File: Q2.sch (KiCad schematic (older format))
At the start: 55 parts, among them U1 LM317, U10 SP-2U1+, U11 SMA, U12 LT1009, U13 TL974, U2 Teensy3.2, U3 SMA, U4 ROS-2536C-119+, U5 PMA4-33GLN+, U6 PGA-103+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

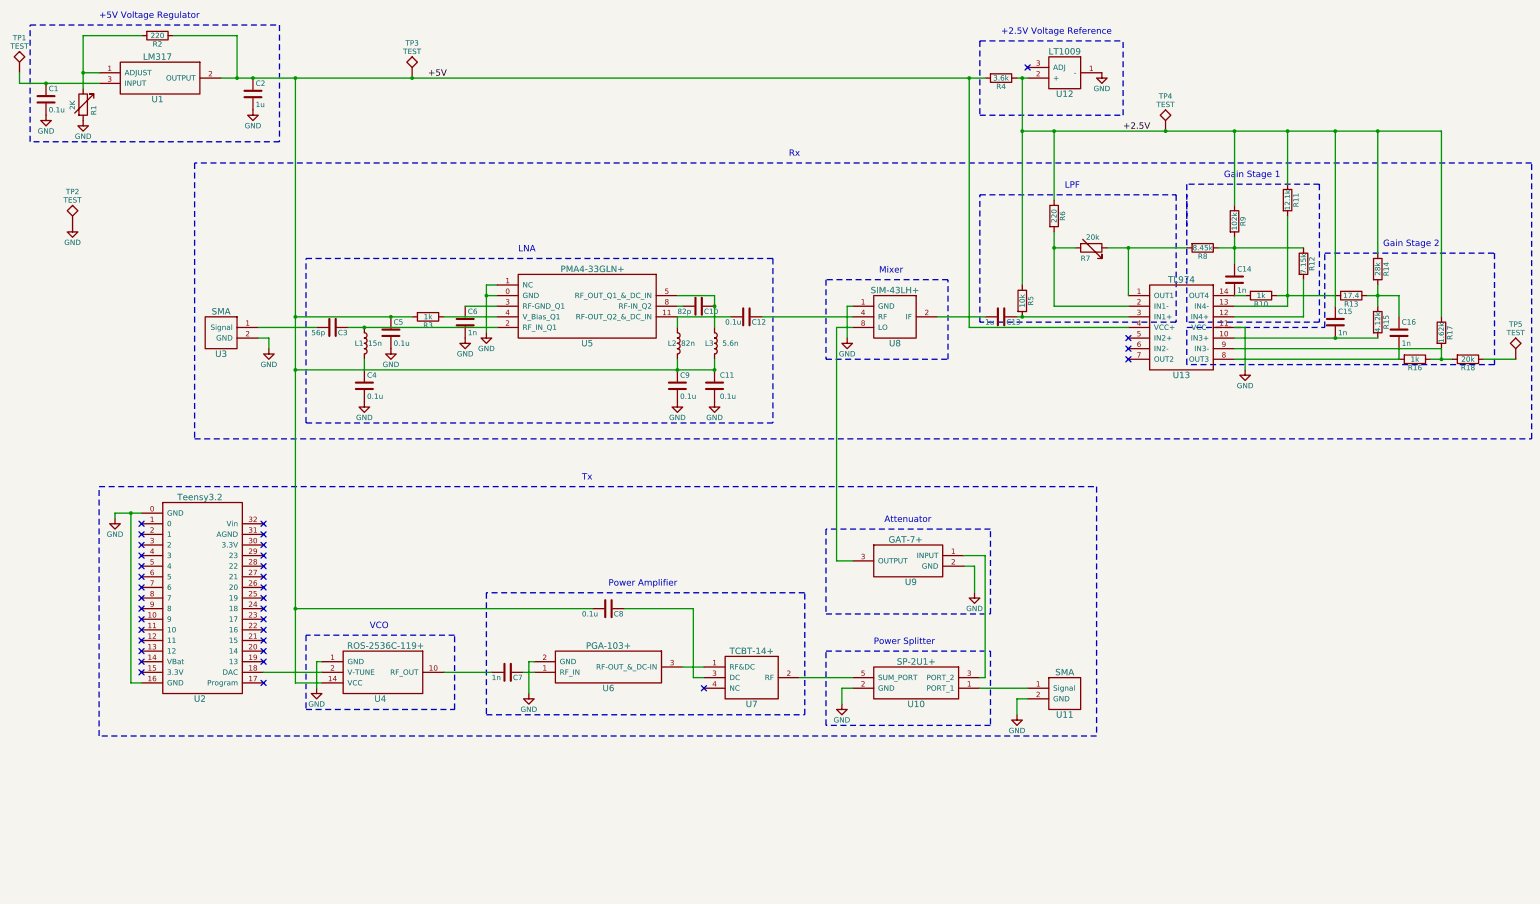
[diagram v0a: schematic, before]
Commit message: Update
Fixed Missing LNA
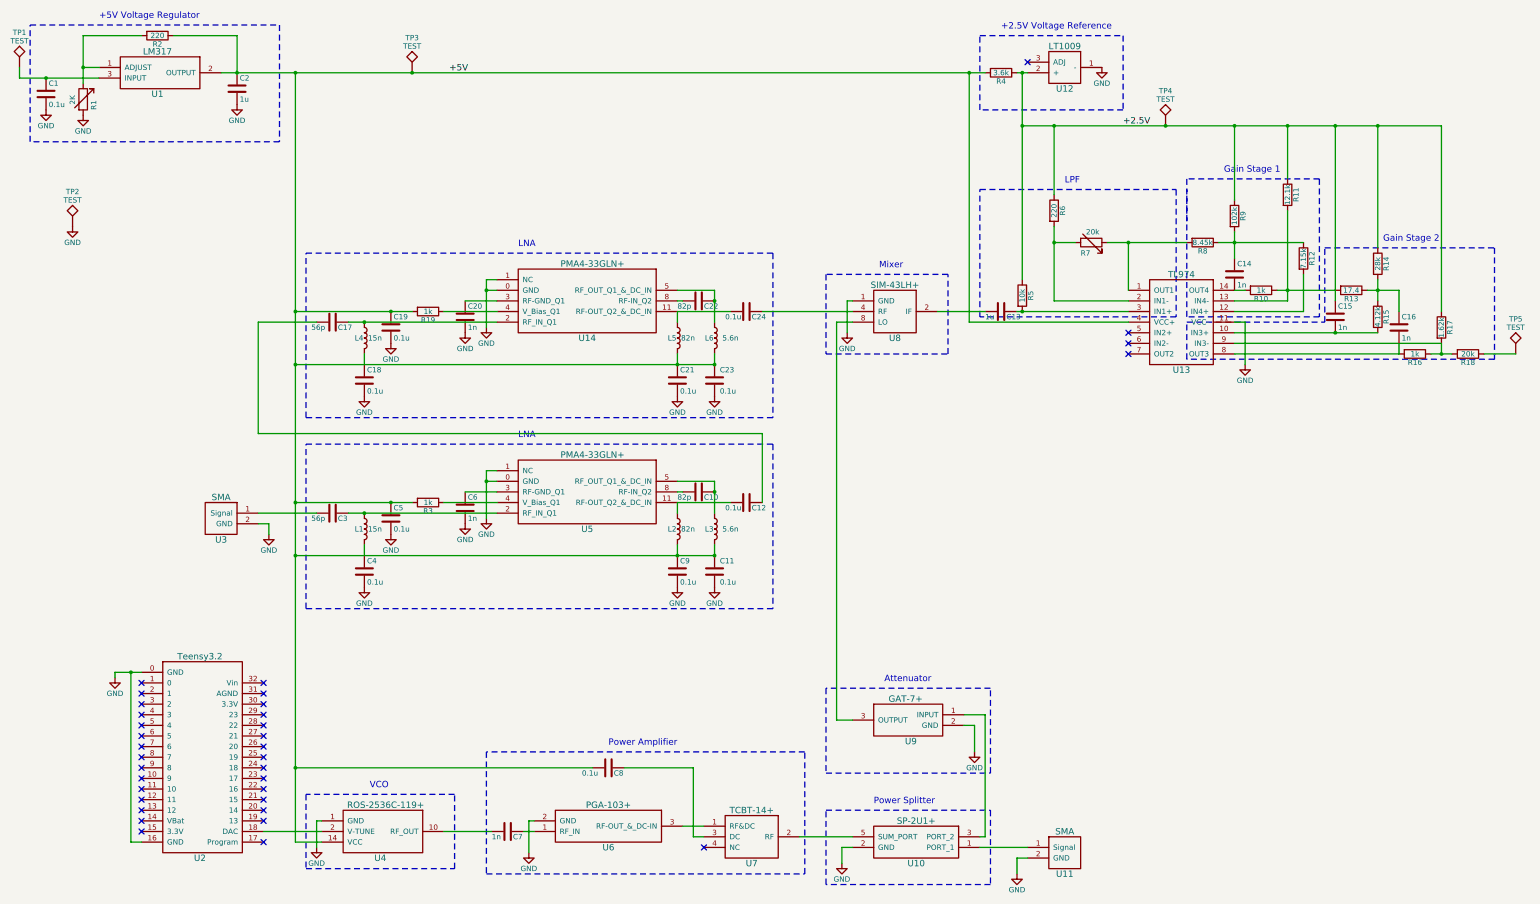
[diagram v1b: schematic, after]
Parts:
- added C17: 56p, Q2Footprint:C_0805_HandSoldering, symbol C
- added C18, C19, C21, C23, C24: 0.1u, Q2Footprint:C_0805_HandSoldering, symbol C
- added C20: 1n, Q2Footprint:C_0805_HandSoldering, symbol C
- added C22: 82p, Q2Footprint:C_0805_HandSoldering, symbol C
- added L4: 15n, Q2Footprint:L_0805_HandSoldering, symbol L
- added L5: 82n, Q2Footprint:L_0805_HandSoldering, symbol L
- added L6: 5.6n, Q2Footprint:L_0805_HandSoldering, symbol L
- added R19: 1k, Q2Footprint:R_0805_HandSoldering, symbol R
- added U14: PMA4-33GLN+, Q2Footprint:PMA4-33GLN+, symbol PMA4-33GLN+
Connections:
- net +5V: now also C19.1, C21.1, C23.1, L5.2, L6.2, R19.2
- net GND: now also C18.2, C19.2, C20.2, C21.2, C23.2, U14.0 (GND), U14.1 (NC)
- net at C12.1: now also C17.2; no longer U8.4 (RF)
- new net: C24.2, L5.1, U14.11 (RF-OUT_Q2_&_DC_IN)
- new net: C17.1, L4.1, U14.2 (RF_IN_Q1)
- new net: C20.1, U14.3 (RF-GND_Q1)
- new net: R19.1, U14.4 (V_Bias_Q1)
- new net: C22.1, L6.1, U14.5 (RF_OUT_Q1_&_DC_IN)
- new net: C22.2, U14.8 (RF-IN_Q2)
- new net: C18.1, L4.2
- new net: C24.1, U8.4 (RF)
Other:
- note removed: "Rx"
- note removed: "Tx"
- moved on the sheet: C1, C10, C11, C12, C13, C14, C15, C16, C2, C3, C4, C5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

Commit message: Update
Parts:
- C12, C24: value 0.1u -> 68p
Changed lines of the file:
@@
 P 7400 5450
 F 0 "C12" V 7450 5500 50  0000 L CNN
-F 1 "0.1u" V 7450 5250 50  0000 L CNN
+F 1 "68p" V 7450 5250 50  0000 L CNN
 F 2 "Q2Footprint:C_0805_HandSoldering" H 7438 5300 50  0001 C CNN
 F 3 "" H 7400 5450 50  0001 C CNN
@@
 P 7400 3650
 F 0 "C24" V 7450 3700 50  0000 L CNN
-F 1 "0.1u" V 7450 3450 50  0000 L CNN
+F 1 "68p" V 7450 3450 50  0000 L CNN
 F 2 "Q2Footprint:C_0805_HandSoldering" H 7438 3500 50  0001 C CNN
 F 3 "" H 7400 3650 50  0001 C CNN

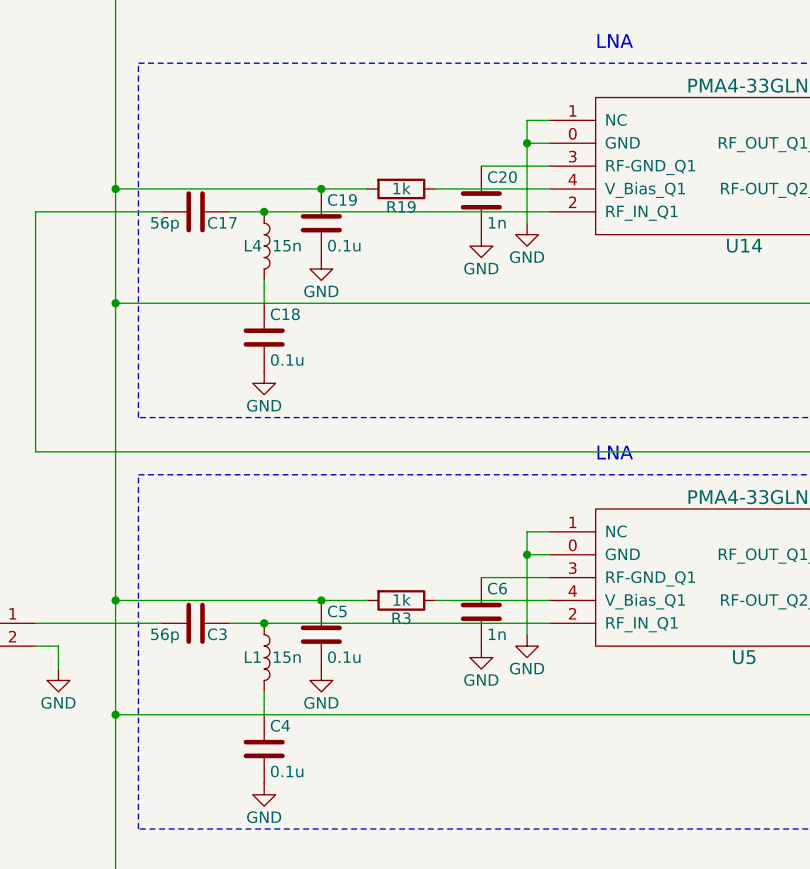
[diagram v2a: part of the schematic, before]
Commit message: Update
Fixed LNA Connection
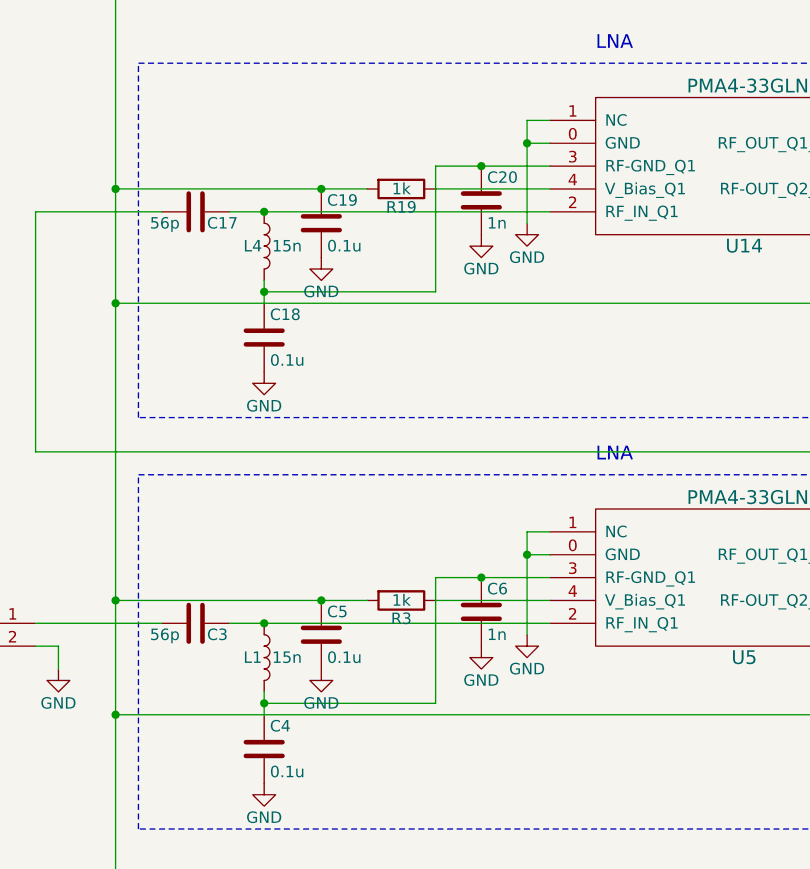
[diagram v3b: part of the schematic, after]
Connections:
- net at C6.1, U5.3 (RF-GND_Q1): now also C4.1, L1.2
- net at C20.1, U14.3 (RF-GND_Q1): now also C18.1, L4.2

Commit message: Update
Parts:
- added C25: 1n, Q2Footprint:C_0805_HandSoldering, symbol C
- R13: value 17.4 -> 17.4k
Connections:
- net +2.5V: now also C25.1
- net at R12.2, U13.12 (IN4+): now also C25.2
- net at C16.2, U13.8 (OUT3): now also R16.1, R18.2; no longer R16.2
- net at R17.2, U13.9 (IN3-): now also R16.2; no longer R16.1, R18.2
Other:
- moved on the sheet: C16, R16, R17
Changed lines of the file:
@@
 P 13100 3450
 F 0 "R13" V 13180 3450 50  0000 C CNN
-F 1 "17.4" V 13100 3450 50  0000 C CNN
+F 1 "17.4k" V 13100 3450 50  0000 C CNN
 F 2 "Q2Footprint:R_0805_HandSoldering" V 13030 3450 50  0001 C CNN
 F 3 "" H 13100 3450 50  0001 C CNN
@@
 L C C16
 U 1 1 5A7C3B98
-P 13550 3800
-F 0 "C16" H 13575 3900 50  0000 L CNN
-F 1 "1n" H 13575 3700 50  0000 L CNN
-F 2 "Q2Footprint:C_0805_HandSoldering" H 13588 3650 50  0001 C CNN
-F 3 "" H 13550 3800 50  0001 C CNN
-	1    13550 3800
+P 13550 3750
+F 0 "C16" H 13575 3850 50  0000 L CNN
+F 1 "1n" H 13575 3650 50  0000 L CNN
+F 2 "Q2Footprint:C_0805_HandSoldering" H 13588 3600 50  0001 C CNN
+F 3 "" H 13550 3750 50  0001 C CNN
+	1    13550 3750
 	1    0    0    -1
 $EndComp
@@
 L R R17
 U 1 1 5A7C5FF9
-P 13950 3800
-F 0 "R17" V 14030 3800 50  0000 C CNN
-F 1 "1.62k" V 13950 3800 50  0000 C CNN
-F 2 "Q2Footprint:R_0805_HandSoldering" V 13880 3800 50  0001 C CNN
-F 3 "" H 13950 3800 50  0001 C CNN
-	1    13950 3800
+P 13900 3450
+F 0 "R17" V 13980 3450 50  0000 C CNN
+F 1 "1.62k" V 13900 3450 50  0000 C CNN
+F 2 "Q2Footprint:R_0805_HandSoldering" V 13830 3450 50  0001 C CNN
+F 3 "" H 13900 3450 50  0001 C CNN
+	1    13900 3450
 	1    0    0    -1
 $EndComp
@@
 L R R16
 U 1 1 5A7C6A64
-P 13700 4050
-F 0 "R16" V 13780 4050 50  0000 C CNN
-F 1 "1k" V 13700 4050 50  0000 C CNN
-F 2 "Q2Footprint:R_0805_HandSoldering" V 13630 4050 50  0001 C CNN
-F 3 "" H 13700 4050 50  0001 C CNN
-	1    13700 4050
-	0    1    1    0
+P 14050 3850
+F 0 "R16" V 14130 3850 50  0000 C CNN
+F 1 "1k" V 14050 3850 50  0000 C CNN
+F 2 "Q2Footprint:R_0805_HandSoldering" V 13980 3850 50  0001 C CNN
+F 3 "" H 14050 3850 50  0001 C CNN
+	1    14050 3850
+	-1   0    0    1
 $EndComp
 $Comp
@@
 	8250 3750 8400 3750
 Wire Wire Line
-	8250 3750 8250 7500
-Wire Wire Line
 	8250 7500 8400 7500
 Wire Wire Line
@@
 	6750 5250 7100 5250
 Wire Wire Line
-	3800 5950 3800 5850
+	3800 5850 3800 5950
 Wire Wire Line
 	14650 4050 14350 4050
 Connection ~ 3800 5550
 Wire Wire Line
-	3800 5550 3800 5550
-Wire Wire Line
 	3650 5550 5050 5550
 Wire Wire Line
@@
 Wire Notes Line
 	12850 3050 14450 3050
-Connection ~ 13950 4050
-Wire Wire Line
-	13950 3950 13950 4050
-Wire Wire Line
-	13850 4050 14050 4050
-Wire Wire Line
-	13950 3950 12000 3950
 Connection ~ 13350 1900
 Wire Wire Line
-	13950 1900 13950 3650
-Wire Wire Line
-	13550 4050 12000 4050
-Wire Wire Line
-	13550 3950 13550 4050
-Wire Wire Line
-	13550 3450 13550 3650
+	13900 1900 13900 3300
+Wire Wire Line
+	12000 4050 14050 4050
 Connection ~ 12950 3850
 Connection ~ 12950 1900
@@
 Wire Wire Line
 	13350 3350 13350 3550
-Wire Wire Line
-	13250 3450 13550 3450
 Wire Notes Line
 	12800 3700 11550 3700
@@
 	10300 1900 10300 2550
 Wire Wire Line
-	10000 1900 13950 1900
+	10000 1900 13900 1900
 Wire Wire Line
 	10800 3000 11550 3000
@@
 	6750 3450 7100 3450
 Wire Wire Line
-	3800 4150 3800 4050
+	3800 4050 3800 4150
 Connection ~ 3800 3750
-Wire Wire Line
-	3800 3750 3800 3750
 Wire Wire Line
 	3650 3750 5050 3750
@@
 Connection ~ 3800 4100
 Connection ~ 4750 3550
+$Comp
+L C C25
+U 1 1 5A7FDE09
+P 12300 2750
+F 0 "C25" H 12325 2850 50  0000 L CNN
+F 1 "1n" H 12325 2650 50  0000 L CNN
+F 2 "Q2Footprint:C_0805_HandSoldering" H 12338 2600 50  0001 C CNN
+F 3 "" H 12300 2750 50  0001 C CNN
+	1    12300 2750
+	1    0    0    -1
+$EndComp
+Wire Wire Line
+	12300 2600 12300 1900
+Connection ~ 12300 1900
+Wire Wire Line
+	12300 2900 12300 3650
+Connection ~ 12300 3650
+Connection ~ 13550 4050
+Wire Wire Line
+	13250 3450 13550 3450
+Wire Wire Line
+	13550 3450 13550 3600
+Wire Wire Line
+	13550 3900 13550 4050
+Wire Wire Line
+	13900 3950 12000 3950
+Wire Wire Line
+	13900 3950 13900 3600
+Wire Wire Line
+	14050 4050 14050 4000
+Wire Wire Line
+	14050 3700 14050 3650
+Wire Wire Line
+	14050 3650 13900 3650
+Connection ~ 13900 3650
+Wire Wire Line
+	8250 3750 8250 7500
 $EndSCHEMATC

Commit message: Update
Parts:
- added TP10, TP11, TP12, TP13, TP14, TP6, TP7, TP8, TP9: TEST, Q2Footprint:PINTST, symbol TEST
- TP1, TP2, TP3, TP4, TP5: footprint Q2Footprint:Test_Point_Keystone_5000-5004_Miniature -> Q2Footprint:PINTST
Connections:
- net at R7.1, R8.2, U13.1 (OUT1): now also TP6.1
- net at C14.2, R10.2, U13.14 (OUT4): now also TP14.1
- net at C13.2, U8.2 (IF): now also TP12.1
- net at C7.2, U4.10 (RF_OUT): now also TP7.1
- net at U10.5 (SUM_PORT), U7.2 (RF): now also TP10.1
- net at C12.1, C17.2: now also TP8.1
- net at C24.1, U8.4 (RF): now also TP9.1
- net at U10.3 (PORT_2), U9.1 (INPUT): now also TP13.1
- net at U8.8 (LO), U9.3 (OUTPUT): now also TP11.1
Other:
- moved on the sheet: R10

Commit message: Update
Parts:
- removed TP10, TP11, TP13, TP7, TP8, TP9: TEST, Q2Footprint:PINTST, symbol TEST
- renumbered TP12 to TP7, TP14 to TP8
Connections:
- net +5V: now also C8.1, U2.32 (Vin), U7.3 (DC); no longer C8.2
- net GND: now also C8.2
- net at C13.1, R5.2, U13.3 (IN1+): now also TP7.1
- net at C13.2, U8.2 (IF): no longer TP7.1
- no-connect marks 35 -> 34
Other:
- moved on the sheet: C8, R5, TP7, U12
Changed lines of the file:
@@
 NoConn ~ 1700 8450
 NoConn ~ 1700 8550
-NoConn ~ 2850 7150
 NoConn ~ 2850 7250
 NoConn ~ 2850 7350
@@
 L LT1009 U12
 U 1 1 5A7B8AA5
-P 10400 1350
-F 0 "U12" H 10400 1150 60  0000 C CNN
-F 1 "LT1009" H 10400 1550 60  0000 C CNN
-F 2 "Q2Footprint:LT1009" H 10300 1350 60  0001 C CNN
-F 3 "" H 10300 1350 60  0001 C CNN
-	1    10400 1350
-	1    0    0    -1
-$EndComp
-NoConn ~ 10050 1300
+P 10450 1350
+F 0 "U12" H 10450 1150 60  0000 C CNN
+F 1 "LT1009" H 10450 1550 60  0000 C CNN
+F 2 "Q2Footprint:LT1009" H 10350 1350 60  0001 C CNN
+F 3 "" H 10350 1350 60  0001 C CNN
+	1    10450 1350
+	1    0    0    -1
+$EndComp
+NoConn ~ 10100 1300
 $Comp
 L R R4
@@
 L GND #PWR05
 U 1 1 5A7B8C7C
-P 10750 1350
-F 0 "#PWR05" H 10750 1100 50  0001 C CNN
-F 1 "GND" H 10750 1200 50  0000 C CNN
-F 2 "" H 10750 1350 50  0001 C CNN
-F 3 "" H 10750 1350 50  0001 C CNN
-	1    10750 1350
+P 10800 1350
+F 0 "#PWR05" H 10800 1100 50  0001 C CNN
+F 1 "GND" H 10800 1200 50  0000 C CNN
+F 2 "" H 10800 1350 50  0001 C CNN
+F 3 "" H 10800 1350 50  0001 C CNN
+	1    10800 1350
 	1    0    0    -1
 $EndComp
@@
 L R R5
 U 1 1 5A7B944E
-P 10000 3500
-F 0 "R5" V 10080 3500 50  0000 C CNN
-F 1 "10k" V 10000 3500 50  0000 C CNN
-F 2 "Q2Footprint:R_0805_HandSoldering" V 9930 3500 50  0001 C CNN
-F 3 "" H 10000 3500 50  0001 C CNN
-	1    10000 3500
+P 10100 3500
+F 0 "R5" V 10180 3500 50  0000 C CNN
+F 1 "10k" V 10100 3500 50  0000 C CNN
+F 2 "Q2Footprint:R_0805_HandSoldering" V 10030 3500 50  0001 C CNN
+F 3 "" H 10100 3500 50  0001 C CNN
+	1    10100 3500
 	1    0    0    -1
 $EndComp
@@
 L C C8
 U 1 1 5A7E4B88
-P 6100 7950
-F 0 "C8" V 6150 8000 50  0000 L CNN
-F 1 "0.1u" V 6150 7700 50  0000 L CNN
-F 2 "Q2Footprint:C_0805_HandSoldering" H 6138 7800 50  0001 C CNN
-F 3 "" H 6100 7950 50  0001 C CNN
-	1    6100 7950
-	0    1    1    0
+P 6900 8750
+F 0 "C8" H 7000 8850 50  0000 L CNN
+F 1 "0.1u" H 6950 8650 50  0000 L CNN
+F 2 "Q2Footprint:C_0805_HandSoldering" H 6938 8600 50  0001 C CNN
+F 3 "" H 6900 8750 50  0001 C CNN
+	1    6900 8750
+	1    0    0    -1
 $EndComp
 Text Notes 6100 7750 0    60   ~ 0
@@
 $Comp
 L TEST TP7
-U 1 1 5A7E6F80
-P 4800 8550
-F 0 "TP7" H 4800 8850 50  0000 C BNN
-F 1 "TEST" H 4800 8800 50  0000 C CNN
-F 2 "Q2Footprint:PINTST" H 4800 8550 50  0001 C CNN
-F 3 "" H 4800 8550 50  0001 C CNN
-	1    4800 8550
-	1    0    0    -1
-$EndComp
-$Comp
-L TEST TP10
-U 1 1 5A7E8283
-P 8050 8600
-F 0 "TP10" H 8050 8900 50  0000 C BNN
-F 1 "TEST" H 8050 8850 50  0000 C CNN
-F 2 "Q2Footprint:PINTST" H 8050 8600 50  0001 C CNN
-F 3 "" H 8050 8600 50  0001 C CNN
-	1    8050 8600
-	1    0    0    -1
-$EndComp
-$Comp
-L TEST TP13
-U 1 1 5A7E8D64
-P 9650 8150
-F 0 "TP13" V 9650 8450 50  0000 C BNN
-F 1 "TEST" V 9700 8450 50  0000 C CNN
-F 2 "Q2Footprint:PINTST" H 9650 8150 50  0001 C CNN
-F 3 "" H 9650 8150 50  0001 C CNN
-	1    9650 8150
-	0    1    1    0
-$EndComp
-$Comp
-L TEST TP11
-U 1 1 5A7E92A3
-P 8250 6900
-F 0 "TP11" V 8250 7200 50  0000 C BNN
-F 1 "TEST" V 8300 7200 50  0000 C CNN
-F 2 "Q2Footprint:PINTST" H 8250 6900 50  0001 C CNN
-F 3 "" H 8250 6900 50  0001 C CNN
-	1    8250 6900
-	0    1    1    0
-$EndComp
-$Comp
-L TEST TP8
-U 1 1 5A7ED2E7
-P 7550 4850
-F 0 "TP8" V 7550 5150 50  0000 C BNN
-F 1 "TEST" V 7600 5150 50  0000 C CNN
-F 2 "Q2Footprint:PINTST" H 7550 4850 50  0001 C CNN
-F 3 "" H 7550 4850 50  0001 C CNN
-	1    7550 4850
-	0    1    1    0
-$EndComp
-$Comp
-L TEST TP9
-U 1 1 5A7ED861
-P 7900 3650
-F 0 "TP9" H 7900 3950 50  0000 C BNN
-F 1 "TEST" H 7900 3900 50  0000 C CNN
-F 2 "Q2Footprint:PINTST" H 7900 3650 50  0001 C CNN
-F 3 "" H 7900 3650 50  0001 C CNN
-	1    7900 3650
-	1    0    0    -1
-$EndComp
-$Comp
-L TEST TP12
 U 1 1 5A7F2511
-P 9400 3650
-F 0 "TP12" H 9400 3950 50  0000 C BNN
-F 1 "TEST" H 9400 3900 50  0000 C CNN
-F 2 "Q2Footprint:PINTST" H 9400 3650 50  0001 C CNN
-F 3 "" H 9400 3650 50  0001 C CNN
-	1    9400 3650
+P 10000 3650
+F 0 "TP7" H 10000 3950 50  0000 C BNN
+F 1 "TEST" H 10000 3900 50  0000 C CNN
+F 2 "Q2Footprint:PINTST" H 10000 3650 50  0001 C CNN
+F 3 "" H 10000 3650 50  0001 C CNN
+	1    10000 3650
 	1    0    0    -1
 $EndComp
@@
 $EndComp
 $Comp
-L TEST TP14
+L TEST TP8
 U 1 1 5A7FD7C4
 P 12150 3450
-F 0 "TP14" H 12300 3650 50  0000 C BNN
+F 0 "TP8" H 12300 3650 50  0000 C BNN
 F 1 "TEST" H 12300 3600 50  0000 C CNN
 F 2 "Q2Footprint:PINTST" H 12150 3450 50  0001 C CNN
@@
 	1    0    0    -1
 $EndComp
-Connection ~ 10000 1400
+Connection ~ 10100 1400
 Wire Wire Line
 	2450 1400 9650 1400
 Wire Wire Line
-	9950 1400 10050 1400
+	9950 1400 10100 1400
 Wire Wire Line
 	10050 8700 9600 8700
@@
 	8400 3550 8350 3550
 Wire Wire Line
-	7550 3650 8400 3650
-Wire Wire Line
 	8250 3750 8400 3750
 Wire Wire Line
@@
 	10050 8800 9950 8800
 Connection ~ 11350 1900
-Wire Wire Line
-	7900 8600 8400 8600
 Wire Notes Line
 	9700 9050 8150 9050
@@
 	7950 7800 4950 7800
 Wire Notes Line
-	7950 8950 7950 7800
-Wire Notes Line
-	4950 8950 7950 8950
-Wire Notes Line
-	4950 7800 4950 8950
+	7950 7800 7950 9100
+Wire Notes Line
+	4950 7800 4950 9100
 Wire Wire Line
 	7000 8500 6800 8500
-Wire Wire Line
-	6900 7950 6250 7950
-Wire Wire Line
-	6900 8600 6900 7950
 Wire Wire Line
 	7000 8600 6900 8600
 Connection ~ 3150 7950
-Wire Wire Line
-	3150 7950 5950 7950
-Wire Wire Line
-	4550 8550 5000 8550
 Wire Wire Line
 	5400 8550 5300 8550
@@
 Wire Notes Line
 	11450 3700 9600 3700
-Connection ~ 10000 1900
-Wire Wire Line
-	10000 1400 10000 3350
+Connection ~ 10100 1900
+Wire Wire Line
+	10100 1400 10100 3350
 Wire Wire Line
 	10300 1900 10300 2550
 Wire Wire Line
-	10000 1900 13900 1900
+	10100 1900 13900 1900
 Wire Wire Line
 	10800 3000 11550 3000
@@
 Connection ~ 3150 4150
 Wire Wire Line
-	7550 4800 7550 5450
-Wire Wire Line
 	7550 4800 2800 4800
 Wire Wire Line
@@
 	14050 3650 13900 3650
 Connection ~ 13900 3650
-Wire Wire Line
-	8250 3750 8250 7500
-Connection ~ 7550 4850
-Connection ~ 9400 3650
-Connection ~ 7900 3650
-Connection ~ 8250 6900
-Connection ~ 9650 8150
-Connection ~ 8050 8600
-Connection ~ 4800 8550
 Connection ~ 11250 3000
 Wire Wire Line
 	12450 3450 12950 3450
+$Comp
+L GND #PWR027
+U 1 1 5A7E37D1
+P 6900 8900
+F 0 "#PWR027" H 6900 8650 50  0001 C CNN
+F 1 "GND" H 6900 8750 50  0000 C CNN
+F 2 "" H 6900 8900 50  0001 C CNN
+F 3 "" H 6900 8900 50  0001 C CNN
+	1    6900 8900
+	1    0    0    -1
+$EndComp
+Wire Notes Line
+	4950 9100 7950 9100
+Wire Wire Line
+	6900 8600 6900 7950
+Wire Wire Line
+	6900 7950 3150 7950
+Wire Wire Line
+	5000 8550 4550 8550
+Wire Wire Line
+	8400 8600 7900 8600
+Wire Wire Line
+	8250 7500 8250 3750
+Wire Wire Line
+	7550 4800 7550 5450
+Wire Wire Line
+	8400 3650 7550 3650
+Wire Wire Line
+	2850 7150 3150 7150
+Connection ~ 3150 7150
+Connection ~ 10100 3650
 $EndSCHEMATC
